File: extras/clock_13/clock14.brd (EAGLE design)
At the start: 57 x 70 mm, 74 parts, among them IC1 VS1838, IC102 ESP32, IC103 ESP32C3-MODULE13U, IC3 IRM-H638T, J101 COM, J102 COM, J107 COM, J2 4P-2.0, K101 SRD-05VDC SL-C, K102 SRD-05VDC SL-C, SW1 PRG, SW101 RST, SW102 PRG, SW103 RST, SW104 RST, SW105 PRG, SW106 PRG, T101 S8050, T102 S8050, U101 AP2112, U102 AP2112, U103 AP2112, X1 SHT22

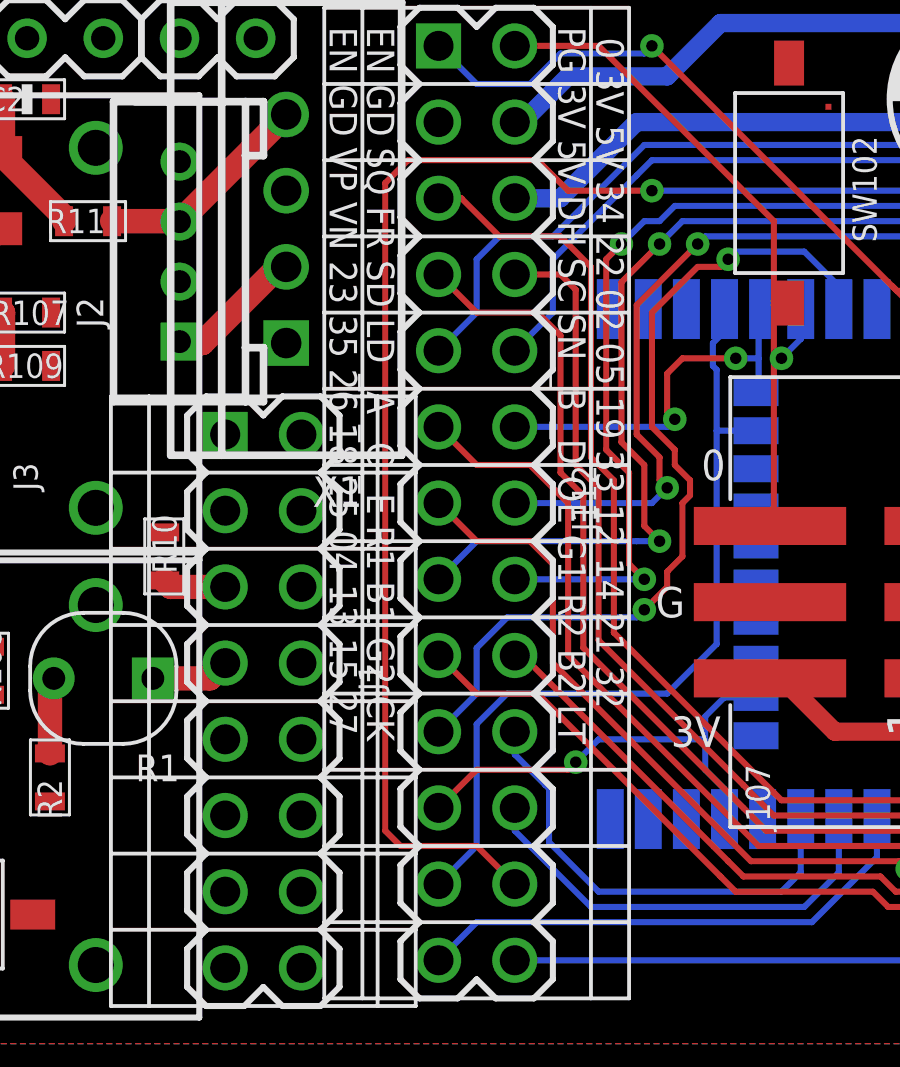
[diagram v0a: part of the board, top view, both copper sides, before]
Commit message: add m7219 test
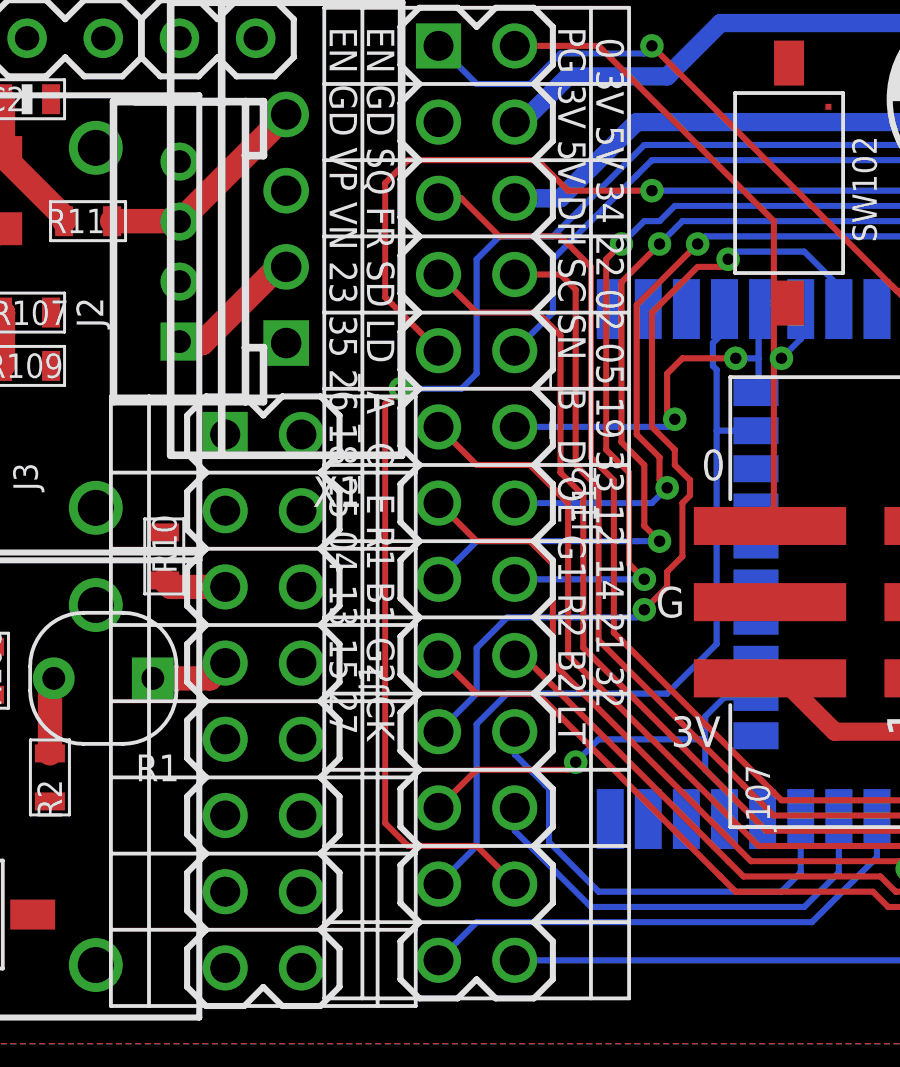
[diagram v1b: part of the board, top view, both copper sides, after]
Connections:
- net 4IO21: now also J112.9; no longer J112.24
- net 4IO23: now also J112.24; no longer J112.9
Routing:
- net 4IO23: track 34.1 -> 56.9 mm, vias 0 -> 1
- net 4IO21: track 53.9 -> 33.6 mm
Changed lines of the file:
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@@
 <signal name="4IO23">
 <contactref element="IC102" pad="37"/>
-<contactref element="J112" pad="9"/>
-<wire x1="4.826" y1="41.91" x2="4.064" y2="41.148" width="0.2032" layer="16"/>
-<wire x1="4.064" y1="41.148" x2="4.064" y2="39.37" width="0.2032" layer="16"/>
-<wire x1="4.064" y1="39.37" x2="2.794" y2="38.1" width="0.2032" layer="16"/>
 <wire x1="6.604" y1="41.91" x2="4.826" y2="41.91" width="0.2032" layer="16"/>
 <wire x1="28.194" y1="42.418" x2="30.106" y2="40.506" width="0.2032" layer="16"/>
@@
 <wire x1="9.652" y1="44.958" x2="19.558" y2="44.958" width="0.2032" layer="16"/>
 <wire x1="19.558" y1="44.958" x2="22.098" y2="42.418" width="0.2032" layer="16"/>
+<contactref element="J112" pad="24"/>
+<wire x1="5.334" y1="20.32" x2="4.064" y2="21.59" width="0.2032" layer="1"/>
+<wire x1="4.064" y1="21.59" x2="1.778" y2="21.59" width="0.2032" layer="1"/>
+<wire x1="1.778" y1="21.59" x2="1.016" y2="22.352" width="0.2032" layer="1"/>
+<wire x1="1.016" y1="22.352" x2="1.016" y2="36.322" width="0.2032" layer="1"/>
+<wire x1="1.016" y1="36.322" x2="1.524" y2="36.83" width="0.2032" layer="1"/>
+<via x="1.524" y="36.83" extent="1-16" drill="0.381"/>
+<wire x1="1.524" y1="36.83" x2="3.556" y2="36.83" width="0.2032" layer="16"/>
+<wire x1="3.556" y1="36.83" x2="4.064" y2="37.338" width="0.2032" layer="16"/>
+<wire x1="4.064" y1="37.338" x2="4.064" y2="41.148" width="0.2032" layer="16"/>
+<wire x1="4.064" y1="41.148" x2="4.826" y2="41.91" width="0.2032" layer="16"/>
 </signal>
 <signal name="4IO5">
@@
 <signal name="4IO21">
 <contactref element="IC102" pad="33"/>
-<contactref element="J112" pad="24"/>
 <wire x1="25.026" y1="39.488" x2="25.026" y2="41.014" width="0.2032" layer="16"/>
 <wire x1="25.026" y1="41.014" x2="24.638" y2="41.402" width="0.2032" layer="16"/>
@@
 <wire x1="6.096" y1="44.45" x2="1.778" y2="44.45" width="0.2032" layer="1"/>
 <wire x1="1.778" y1="44.45" x2="1.016" y2="43.688" width="0.2032" layer="1"/>
-<wire x1="1.016" y1="43.688" x2="1.016" y2="22.098" width="0.2032" layer="1"/>
-<wire x1="1.016" y1="22.098" x2="1.524" y2="21.59" width="0.2032" layer="1"/>
-<wire x1="1.524" y1="21.59" x2="4.064" y2="21.59" width="0.2032" layer="1"/>
-<wire x1="4.064" y1="21.59" x2="5.334" y2="20.32" width="0.2032" layer="1"/>
+<contactref element="J112" pad="9"/>
+<wire x1="1.016" y1="43.688" x2="1.016" y2="39.878" width="0.2032" layer="1"/>
+<wire x1="1.016" y1="39.878" x2="2.794" y2="38.1" width="0.2032" layer="1"/>
 </signal>
 <signal name="4EN">

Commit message: sss
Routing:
- net 4IO23: track 56.9 -> 59.9 mm
- net 4IO12: track 15.3 -> 14.0 mm, vias 0 -> 1
- net 4IO15: track 27.9 -> 28.0 mm, vias 0 -> 1
- net 4IO13: vias 1 -> 0
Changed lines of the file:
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@@
 <wire x1="19.558" y1="44.958" x2="22.098" y2="42.418" width="0.2032" layer="16"/>
 <contactref element="J112" pad="24"/>
-<wire x1="5.334" y1="20.32" x2="4.064" y2="21.59" width="0.2032" layer="1"/>
-<wire x1="4.064" y1="21.59" x2="1.778" y2="21.59" width="0.2032" layer="1"/>
-<wire x1="1.778" y1="21.59" x2="1.016" y2="22.352" width="0.2032" layer="1"/>
-<wire x1="1.016" y1="22.352" x2="1.016" y2="36.322" width="0.2032" layer="1"/>
-<wire x1="1.016" y1="36.322" x2="1.524" y2="36.83" width="0.2032" layer="1"/>
-<via x="1.524" y="36.83" extent="1-16" drill="0.381"/>
-<wire x1="1.524" y1="36.83" x2="3.556" y2="36.83" width="0.2032" layer="16"/>
+<wire x1="1.016" y1="19.304" x2="1.016" y2="36.576" width="0.2032" layer="1"/>
+<wire x1="1.016" y1="36.576" x2="1.27" y2="36.83" width="0.2032" layer="1"/>
+<via x="1.27" y="36.83" extent="1-16" drill="0.381"/>
+<wire x1="1.27" y1="36.83" x2="3.556" y2="36.83" width="0.2032" layer="16"/>
 <wire x1="3.556" y1="36.83" x2="4.064" y2="37.338" width="0.2032" layer="16"/>
 <wire x1="4.064" y1="37.338" x2="4.064" y2="41.148" width="0.2032" layer="16"/>
 <wire x1="4.064" y1="41.148" x2="4.826" y2="41.91" width="0.2032" layer="16"/>
+<wire x1="1.016" y1="19.304" x2="1.27" y2="19.05" width="0.2032" layer="1"/>
+<wire x1="1.27" y1="19.05" x2="4.064" y2="19.05" width="0.2032" layer="1"/>
+<wire x1="4.064" y1="19.05" x2="5.334" y2="20.32" width="0.2032" layer="1"/>
 </signal>
 <signal name="4IO5">
@@
 <contactref element="J112" pad="23"/>
 <wire x1="12.326" y1="39.488" x2="12.326" y2="39.504" width="0.2032" layer="16"/>
-<wire x1="2.794" y1="20.32" x2="4.064" y2="21.59" width="0.2032" layer="16"/>
-<wire x1="4.064" y1="21.59" x2="4.064" y2="25.654" width="0.2032" layer="16"/>
+<wire x1="2.794" y1="20.32" x2="4.064" y2="21.59" width="0.2032" layer="1"/>
+<wire x1="4.064" y1="21.59" x2="4.064" y2="25.908" width="0.2032" layer="1"/>
 <wire x1="12.326" y1="39.504" x2="12.192" y2="39.37" width="0.2032" layer="16"/>
 <wire x1="13.376" y1="35.433" x2="12.065" y2="35.433" width="0.2032" layer="16"/>
@@
 <wire x1="11.938" y1="38.354" x2="12.326" y2="38.742" width="0.2032" layer="16"/>
 <wire x1="12.326" y1="39.488" x2="12.326" y2="38.742" width="0.2032" layer="16"/>
-<wire x1="5.08" y1="26.67" x2="4.064" y2="25.654" width="0.2032" layer="16"/>
-<wire x1="5.08" y1="26.67" x2="10.414" y2="26.67" width="0.2032" layer="16"/>
+<wire x1="4.826" y1="26.67" x2="4.064" y2="25.908" width="0.2032" layer="16"/>
+<wire x1="4.826" y1="26.67" x2="10.414" y2="26.67" width="0.2032" layer="16"/>
 <wire x1="10.414" y1="26.67" x2="12.065" y2="28.321" width="0.2032" layer="16"/>
 <wire x1="12.065" y1="35.433" x2="12.065" y2="28.321" width="0.2032" layer="16"/>
+<via x="4.064" y="25.908" extent="1-16" drill="0.381"/>
 </signal>
 <signal name="4IO35">
@@
 <contactref element="J112" pad="17"/>
 <via x="19.812" y="20.066" extent="1-16" drill="0.381"/>
-<wire x1="6.096" y1="26.67" x2="4.064" y2="26.67" width="0.2032" layer="1"/>
-<wire x1="4.064" y1="26.67" x2="2.794" y2="27.94" width="0.2032" layer="1"/>
+<wire x1="6.096" y1="26.67" x2="5.08" y2="26.67" width="0.2032" layer="1"/>
 <wire x1="6.096" y1="26.67" x2="12.192" y2="20.574" width="0.2032" layer="1"/>
 <wire x1="19.946" y1="22.488" x2="19.946" y2="22.486" width="0.2032" layer="16"/>
@@
 <wire x1="17.78" y1="19.558" x2="19.304" y2="19.558" width="0.2032" layer="1"/>
 <wire x1="19.304" y1="19.558" x2="19.812" y2="20.066" width="0.2032" layer="1"/>
+<wire x1="2.794" y1="27.94" x2="3.81" y2="27.94" width="0.2032" layer="1"/>
+<wire x1="3.81" y1="27.94" x2="5.08" y2="26.67" width="0.2032" layer="1"/>
 </signal>
 <signal name="4IO33">
@@
 <wire x1="16.136" y1="22.488" x2="16.136" y2="20.708" width="0.2032" layer="16"/>
 <wire x1="16.136" y1="20.708" x2="14.986" y2="19.558" width="0.2032" layer="16"/>
-<wire x1="14.986" y1="19.558" x2="7.874" y2="19.558" width="0.2032" layer="16"/>
-<wire x1="5.334" y1="22.86" x2="5.334" y2="22.098" width="0.2032" layer="16"/>
-<wire x1="5.334" y1="22.098" x2="7.874" y2="19.558" width="0.2032" layer="16"/>
+<wire x1="14.986" y1="19.558" x2="8.636" y2="19.558" width="0.2032" layer="16"/>
+<wire x1="5.334" y1="22.86" x2="6.096" y2="22.098" width="0.2032" layer="16"/>
+<wire x1="6.096" y1="22.098" x2="8.636" y2="19.558" width="0.2032" layer="16"/>
 </signal>
 <signal name="4IO12">
@@
 <wire x1="14.866" y1="22.488" x2="14.866" y2="20.708" width="0.2032" layer="16"/>
 <wire x1="14.866" y1="20.708" x2="14.224" y2="20.066" width="0.2032" layer="16"/>
-<wire x1="14.224" y1="20.066" x2="8.128" y2="20.066" width="0.2032" layer="16"/>
-<wire x1="8.128" y1="20.066" x2="6.477" y2="21.717" width="0.2032" layer="16"/>
-<wire x1="5.334" y1="25.4" x2="5.334" y2="24.638" width="0.2032" layer="16"/>
-<wire x1="5.334" y1="24.638" x2="6.35" y2="23.622" width="0.2032" layer="16"/>
-<wire x1="6.477" y1="21.717" x2="6.477" y2="23.495" width="0.2032" layer="16"/>
-<wire x1="6.477" y1="23.495" x2="6.35" y2="23.622" width="0.2032" layer="16"/>
+<via x="11.303" y="20.32" extent="1-16" drill="0.381"/>
+<wire x1="14.224" y1="20.066" x2="11.557" y2="20.066" width="0.2032" layer="16"/>
+<wire x1="11.557" y1="20.066" x2="11.303" y2="20.32" width="0.2032" layer="16"/>
+<wire x1="5.334" y1="25.4" x2="6.604" y2="25.4" width="0.254" layer="1"/>
+<wire x1="6.604" y1="25.4" x2="11.303" y2="20.701" width="0.254" layer="1"/>
+<wire x1="11.303" y1="20.701" x2="11.303" y2="20.32" width="0.254" layer="1"/>
 </signal>
 <signal name="4IO13">
@@
 <wire x1="11.684" y1="25.908" x2="12.319" y2="26.543" width="0.2032" layer="16"/>
 <wire x1="13.376" y1="26.543" x2="12.319" y2="26.543" width="0.2032" layer="16"/>
-<via x="7.366" y="24.384" extent="1-16" drill="0.381"/>
-<wire x1="4.064" y1="24.13" x2="2.794" y2="22.86" width="0.2032" layer="1"/>
-<wire x1="7.366" y1="24.384" x2="8.128" y2="25.146" width="0.2032" layer="16"/>
-<wire x1="8.128" y1="25.146" x2="11.684" y2="25.146" width="0.2032" layer="16"/>
-<wire x1="4.064" y1="24.13" x2="7.112" y2="24.13" width="0.2032" layer="1"/>
-<wire x1="7.112" y1="24.13" x2="7.366" y2="24.384" width="0.2032" layer="1"/>
+<wire x1="4.064" y1="24.13" x2="2.794" y2="22.86" width="0.2032" layer="16"/>
+<wire x1="5.588" y1="24.13" x2="6.604" y2="25.146" width="0.2032" layer="16"/>
+<wire x1="6.604" y1="25.146" x2="11.684" y2="25.146" width="0.2032" layer="16"/>
+<wire x1="4.064" y1="24.13" x2="5.588" y2="24.13" width="0.2032" layer="16"/>
 </signal>
 <signal name="4SVN">
@@
 <wire x1="9.398" y1="29.21" x2="5.08" y2="29.21" width="0.2032" layer="16"/>
 <wire x1="5.08" y1="29.21" x2="4.064" y2="28.194" width="0.2032" layer="16"/>
-<wire x1="4.064" y1="28.194" x2="4.064" y2="26.67" width="0.2032" layer="16"/>
-<wire x1="4.064" y1="26.67" x2="2.794" y2="25.4" width="0.2032" layer="16"/>
 <via x="12.446" y="41.148" extent="1-16" drill="0.381"/>
 <wire x1="12.7" y1="41.402" x2="12.446" y2="41.148" width="0.2032" layer="16"/>
@@
 <wire x1="16.136" y1="39.488" x2="16.136" y2="40.252" width="0.2032" layer="16"/>
 <wire x1="16.136" y1="40.252" x2="16.002" y2="40.386" width="0.2032" layer="16"/>
+<wire x1="2.794" y1="25.4" x2="2.794" y2="26.416" width="0.2032" layer="16"/>
+<wire x1="2.794" y1="26.416" x2="4.064" y2="27.686" width="0.2032" layer="16"/>
+<wire x1="4.064" y1="27.686" x2="4.064" y2="28.194" width="0.2032" layer="16"/>
 </signal>
 <signal name="1EN_P">

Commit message: 1111
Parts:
- removed C104: 500u, radiva5:CPOL-RADIAL-100UF-25V
- removed IC102: ESP32, radiva5:ESP32-WROOVER/WROOM
- removed IC103: ESP32C3-MODULE13U, radiva5:ESP32C3-13U
- removed J102: COM, radiva5:2X03_SMT
- removed J109: (no value), radiva5:USB-B-MICRO-SMD_MY
- removed J111: (no value), radiva5:2X8
- removed R102, R109, R112: 10k, radiva5:R0603
- removed R104: 100k, radiva5:R0603
- removed R107: (no value), radiva5:R0603
- removed SW104: RST, radiva5:MICROPUSH-BUT_TOP
- added C17: 4.7u, radiva5:0603-CAP
- added IC4: VS1838, radiva5:IR
- added IC5: IRM-H638T, radiva5:IRM-H638T
- added J11: (no value), radiva5:1X02
- added J14: (no value), radiva5:2X8
- added J16: 4P-2.0, radiva5:HW4-2.0
- added R12, R17, R5: 10k, radiva5:R0603
- added R14: PHOTORESISTOR-5528-10K, radiva5:SNR2-3.0
- added R16: 100, radiva5:R0603
- added SW7: PRG, radiva5:MICROPUSH-BUT_TOP
- C2: value 4.7u -> 500u; device radiva5:0603-CAP -> radiva5:CPOL-RADIAL-100UF-25V
- IC1: value VS1838 -> ESP32C3-MODULE13U; device radiva5:IR -> radiva5:ESP32C3-13U
- IC2: value (none) -> ESP8266
- IC3: value IRM-H638T -> ESP32; device radiva5:IRM-H638T -> radiva5:ESP32-WROOVER/WROOM
- J1: value (none) -> COM; device radiva5:2X8 -> radiva5:2X03_SMT
- J2: value 4P-2.0 -> (none); device radiva5:HW4-2.0 -> radiva5:2X8
- J3: device radiva5:1X02 -> radiva5:USB-B-MICRO-SMD_MY
- R1: value PHOTORESISTOR-5528-10K -> 10k; device radiva5:SNR2-3.0 -> radiva5:R0603
- R11: value 100 -> (none)
- R2: value 10k -> 100k
- SW1: value PRG -> RST
- moved C2 74.3 mm to (28.4, -16.5), turned to 90 degrees
- moved IC1 60.7 mm to (23.1, -3.05), flipped to the bottom
- moved R1 53.9 mm to (30.0, -10.7), turned to 270 degrees
- moved J2 47.9 mm to (10.7, -3.56), turned to 270 degrees
- moved R2 43.4 mm to (30.0, 7.37), turned to 0 degrees
- moved IC3 40.8 mm to (23.9, 31.0), flipped to the bottom, turned to 90 degrees
- moved J3 40.2 mm to (22.1, 13.7), flipped to the bottom, turned to 90 degrees
- moved J1 39.7 mm to (23.9, -2.79), turned to 180 degrees
- moved SW1 35.7 mm to (19.3, 8.64)
- moved R3 12.6 mm to (-20.8, 11.7), turned to 90 degrees
- moved R10 7.82 mm to (-10.9, 37.6), turned to 0 degrees
- moved R11 3.66 mm to (-10.9, 39.4), turned to 180 degrees
- renumbered C101 to C7, C102 to C6, C103 to C11, C105 to C3, C106 to C14, C107 to C12, C108 to C15, C109 to C8, C110 to C4, C111 to C10, C112 to C16, C113 to C5, C114 to C13, C115 to C9, C116 to C1, D101 to D2, D102 to D1, IC101 to IC2, J101 to J6, J103 to J13, J104 to J12, J105 to J10, J106 to J9, J107 to J7, J108 to J5, J112 to J8, J113 to J4, K101 to K2, K102 to K1, R101 to R4, R103 to R8, R105 to R7, R106 to R15, R108 to R13, R110 to R9, R111 to R6, SJ101 to SJ1, SJ102 to SJ3, SJ103 to SJ2, SW101 to SW5, SW102 to SW6, SW103 to SW3, SW105 to SW4, SW106 to SW2, T101 to T2, T102 to T1, U101 to U2, U102 to U1, U103 to U3, X1 to J15
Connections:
- net +3V3_1: now also IC4.P$3, J14.4, J16.3, R12.1, R16.2, R17.1; no longer IC1.P$3, J1.4, J2.3, R10.1, R11.2, R2.1
- net +3V3_2: now also C2.1, IC1.3V3, J1.2, J2.4, R1.2; no longer C104.1, IC103.3V3, J102.2, J111.4, R112.2
- net +3V3_3: now also R5.1; no longer R3.1
- net +3V3_4: now also IC3.2; no longer IC102.2
- net +5V_1: now also J11.2, J14.6; no longer J1.6, J3.2
- net +5V_2: now also J2.6, J3.VBUS, R2.1; no longer J109.VBUS, J111.6, R104.1
- net 1ADC: now also J14.7, R14.1; no longer J1.7, R1.1
- net 1EN: now also J14.1; no longer J1.1
- net 1IO0: now also J14.2; no longer J1.2
- net 1IO12: now also IC4.P$1, IC5.OUT, J14.5, R17.2; no longer IC1.P$1, IC3.OUT, J1.5, R10.2
- net 1IO13: now also J14.16; no longer J1.16
- net 1IO14: now also J14.15, R10.2; no longer J1.15, R109.2
- net 1IO15: now also J14.12; no longer J1.12
- net 1IO16: now also J14.14; no longer J1.14
- net 1IO2: now also J14.8, SW7.B; no longer J1.8, SW1.B
- net 1IO4: now also J14.9, J16.2; no longer J1.9, J2.2
- net 1IO5: now also J14.10, J16.1; no longer J1.10, J2.1
- net 2D+: now also IC1.IO19, J3.D+; no longer IC103.IO19, J109.D+
- net 2D-: now also IC1.IO18, J3.D-; no longer IC103.IO18, J109.D-
- net 2EN: now also IC1.EN, J1.1, J2.1, R1.1, SW1.B; no longer IC103.EN, J102.1, J111.1, R112.1, SW104.B
- net 2EN_P: now also R2.2; no longer R104.2
- net 2IO0: now also IC1.IO0, J2.8; no longer IC103.IO0, J111.8
- net 2IO1: now also IC1.IO1, J2.7; no longer IC103.IO1, J111.7
- net 2IO10: now also IC1.IO10, J2.15; no longer IC103.IO10, J111.15
- net 2IO2: now also IC1.IO2, J2.5; no longer IC103.IO2, J111.5
- net 2IO3: now also IC1.IO3, J2.12; no longer IC103.IO3, J111.12
- net 2IO4: now also IC1.IO4; no longer IC103.IO4
- net 2IO5: now also IC1.IO5, J2.9; no longer IC103.IO5, J111.9
- net 2IO6: now also IC1.IO6, J2.10; no longer IC103.IO6, J111.10
- net 2IO7: now also IC1.IO7, J2.16; no longer IC103.IO7, J111.16
- net 2IO8: now also IC1.IO8, J2.14; no longer IC103.IO8, J111.14
- net 2IO9: now also IC1.IO9, J1.6, J2.2; no longer IC103.IO9, J102.6, J111.2
- net 2RX0: now also IC1.RX0, J1.5; no longer IC103.RX0, J102.5
- net 2TX0: now also IC1.TX0, J1.3; no longer IC103.TX0, J102.3
- net 3ADC: now also R3.1; no longer R102.1
- net 3IO2: now also R5.2; no longer R3.2
- net 4EN: now also IC3.3; no longer IC102.3
- net 4IO0: now also IC3.25; no longer IC102.25
- net 4IO12: now also IC3.14; no longer IC102.14
- net 4IO13: now also IC3.16, IC3.40; no longer IC102.16, IC102.40
- net 4IO14: now also IC3.13; no longer IC102.13
- net 4IO15: now also IC3.23, IC3.47; no longer IC102.23, IC102.47
- net 4IO16: now also IC3.27; no longer IC102.27
- net 4IO17: now also IC3.28; no longer IC102.28
- net 4IO18: now also IC3.30; no longer IC102.30
- net 4IO19: now also IC3.31; no longer IC102.31
- net 4IO2: now also IC3.24, IC3.48; no longer IC102.24, IC102.48
- net 4IO21: now also IC3.33; no longer IC102.33
- net 4IO22: now also IC3.36; no longer IC102.36
- net 4IO23: now also IC3.37; no longer IC102.37
- net 4IO25: now also IC3.10; no longer IC102.10
- net 4IO26: now also IC3.11; no longer IC102.11
- net 4IO27: now also IC3.12; no longer IC102.12
- net 4IO32: now also IC3.8; no longer IC102.8
- net 4IO33: now also IC3.9; no longer IC102.9
- net 4IO34: now also IC3.6; no longer IC102.6
- net 4IO35: now also IC3.7; no longer IC102.7
- net 4IO4: now also IC3.26; no longer IC102.26
- net 4IO5: now also IC3.29; no longer IC102.29
- net 4RX0: now also IC3.34; no longer IC102.34
- net 4SVN: now also IC3.5; no longer IC102.5
- net 4SVP: now also IC3.4; no longer IC102.4
- net 4TX0: now also IC3.35; no longer IC102.35
- net GND: now also C17.2, IC1.GND, IC3.1, IC3.15, IC3.38, IC3.39, IC3.PAD$1, IC3.PAD$4, IC3.PAD$5, IC3.PAD$7, IC3.PAD$8, IC3.PAD$9, IC4.P$2, IC5.GND, IC5.GND1, J1.4, J11.1, J14.3, J16.4, J2.3, J3.GND, J3.SH@1, J3.SH@2, J3.SH@3, J3.SH@4, J3.SH@5, J3.SH@6, R11.1, R3.2, SW7.A, SW7.SH0; no longer C104.2, IC1.P$2, IC102.1, IC102.15, IC102.38, IC102.39, IC102.GND, IC102.PAD$1, IC102.PAD$4, IC102.PAD$5, IC102.PAD$7, IC102.PAD$8, IC102.PAD$9, IC103.GND, IC3.GND1, J1.3, J102.4, J109.GND, J109.SH@1, J109.SH@2, J109.SH@3, J109.SH@4, J109.SH@5, J109.SH@6, J111.3, J2.4, J3.1, R102.2, R107.1, SW104.A, SW104.SH0
- net IN2_A: now also J2.13; no longer J111.13
- net IN2_LED: now also J2.11; no longer J111.11
- net N$10: now also R12.2, R14.2; no longer R1.2, R2.2
- net N$15: now also C17.1, IC5.VCC, R16.1; no longer C2.1, IC3.VCC, R11.1
- net N$3: now also R10.1, R11.2; no longer R107.2, R109.1
